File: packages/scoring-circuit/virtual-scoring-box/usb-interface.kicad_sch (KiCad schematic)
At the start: 8 parts, among them J1 GCT USB4105-GF-A, U18 ISOUSB111DWR, U3 TPD2E2U06DCKR

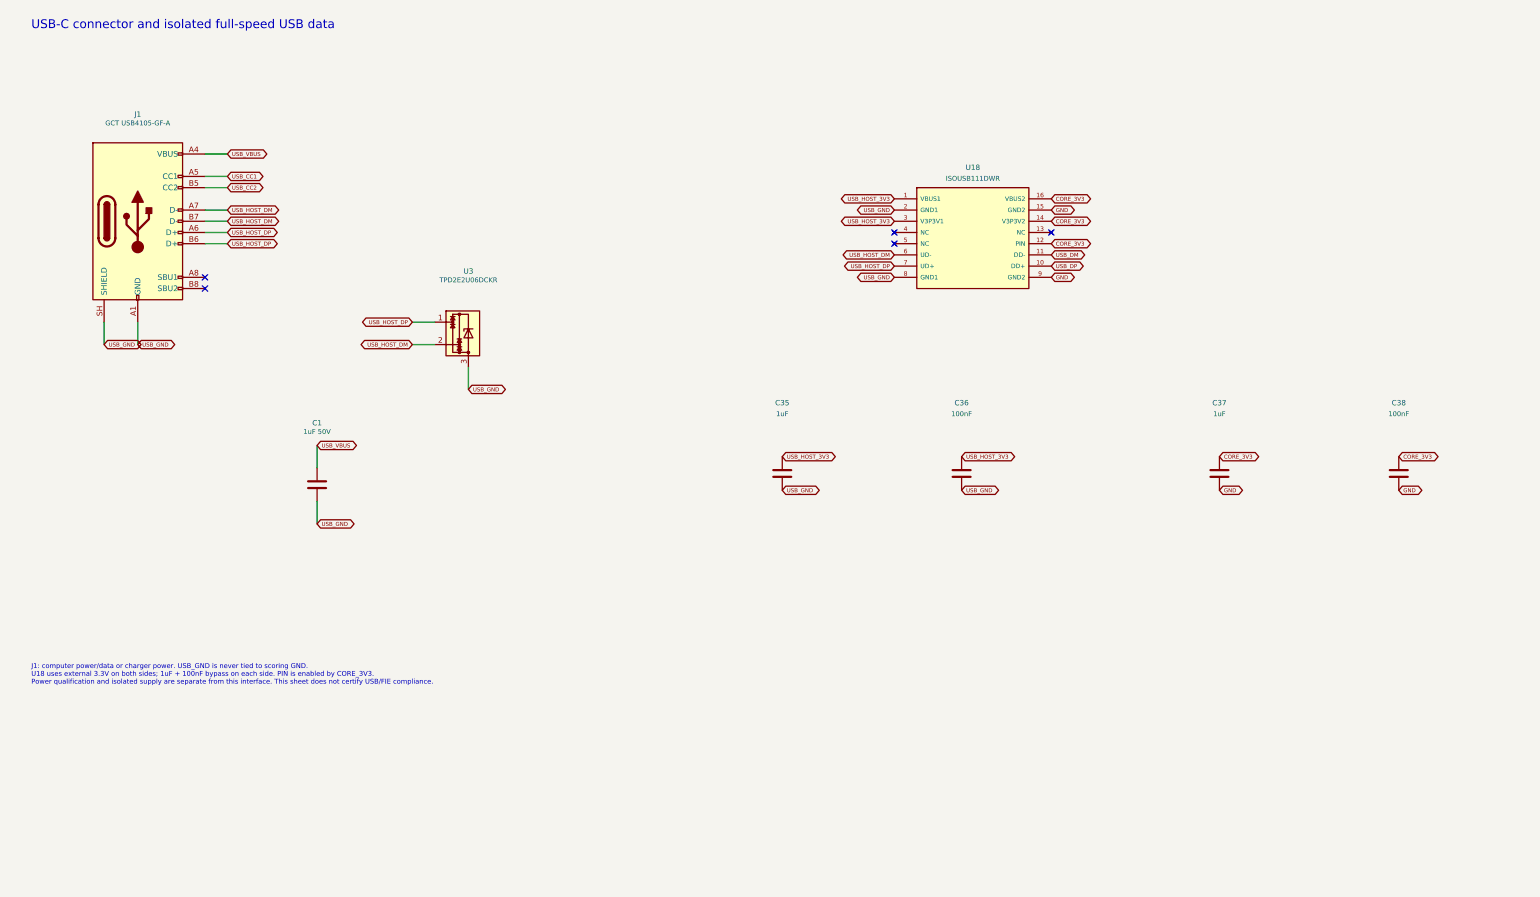
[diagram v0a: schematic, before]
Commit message: feat(scoring-circuit): add suspend-aware isolated serial interface
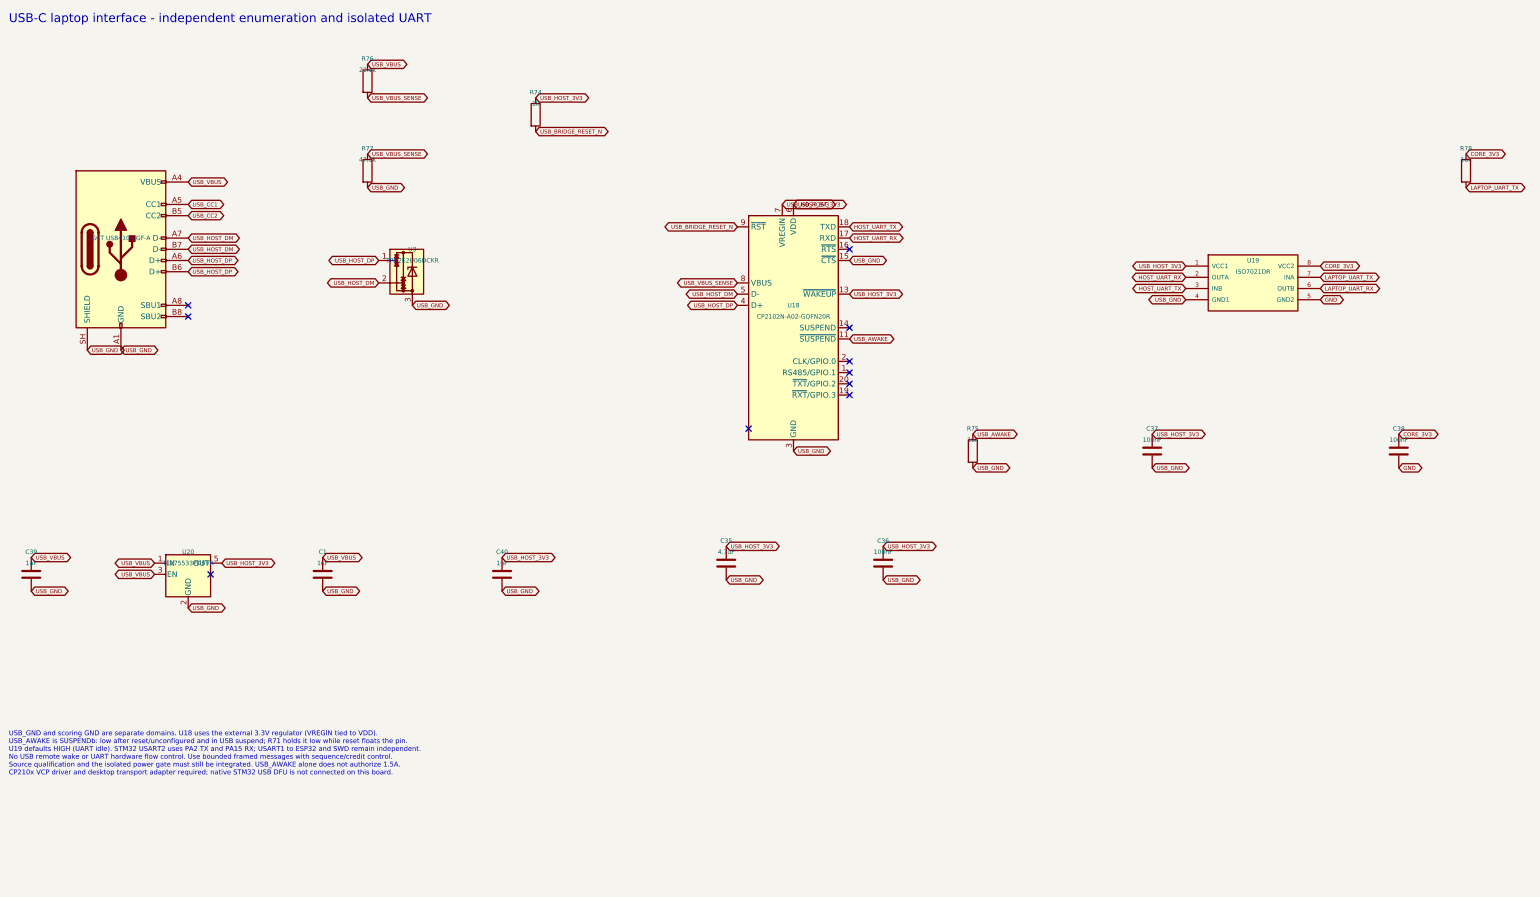
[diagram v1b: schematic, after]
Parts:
- added C39, C40: 1uF, Capacitor_SMD:C_0603_1608Metric, symbol Device:C
- added R74: 1k, Resistor_SMD:R_0603_1608Metric, symbol Device:R
- added R75, R78: 10k, Resistor_SMD:R_0603_1608Metric, symbol Device:R
- added R76: 22.1k, Resistor_SMD:R_0603_1608Metric, symbol Device:R
- added R77: 47.5k, Resistor_SMD:R_0603_1608Metric, symbol Device:R
- added U19: ISO7021DR, Package_SO:SOIC-8_3.9x4.9mm_P1.27mm, symbol ScoringPlatform:ISO7021
- added U20: TLV75533PDBVR, Package_TO_SOT_SMD:SOT-23-5, symbol Regulator_Linear:TLV75533PDBV
- C1: value 1uF 50V -> 1uF; Manufacturer TDK -> (none)
- C35: value 1uF -> 4.7uF; MPN C1608X7R1H105K080AB -> GRM188R61A475KE15D; Manufacturer TDK -> (none)
- C36, C38: Manufacturer Yageo -> (none)
- C37: value 1uF -> 100nF; MPN C1608X7R1H105K080AB -> CC0603KRX7R9BB104; Manufacturer TDK -> (none)
- U18: value ISOUSB111DWR -> CP2102N-A02-GQFN20R; footprint Package_SO:SOIC-16W_7.5x10.3mm_P1.27mm -> ScoringPlatform:CP2102N_QFN20; symbol ScoringPlatform:ISOUSB111 -> Interface_USB:CP2102N-Axx-xQFN20; MPN ISOUSB111DWR -> CP2102N-A02-GQFN20R; Manufacturer Texas Instruments -> Silicon Labs
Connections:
- net CORE_3V3: now also R78.1, U19.8 (VCC2); no longer C37.1, U18.12 (PIN), U18.14 (V3P3V2), U18.16 (VBUS2)
- net GND: now also U19.5 (GND2); no longer C37.2, U18.15 (GND2), U18.9 (GND2)
- net USB_GND: now also C37.2, U18.12 (GND), U18.15 (~{CTS}), U18.21 (GND), U18.3 (GND), C39.2, C40.2, R75.2, R77.2, U19.4 (GND1), U20.2 (GND); no longer U18.2 (GND1), U18.8 (GND1)
- net USB_HOST_3V3: now also C37.1, U18.13 (~{WAKEUP}), U18.6 (VDD), U18.7 (VREGIN), C40.1, R74.1, U19.1 (VCC1), U20.5 (OUT); no longer U18.1 (VBUS1), U18.3 (V3P3V1)
- net USB_HOST_DM: now also U18.5 (D-); no longer U18.6 (UD-)
- net USB_HOST_DP: now also U18.4 (D+); no longer U18.7 (UD+)
- net USB_VBUS: now also C39.1, R76.1, U20.1 (IN), U20.3 (EN)
- net USB_DM renamed USB_AWAKE
- net USB_AWAKE: now also R75.1
- net USB_DP: no longer names the net of U18.10 (NC)
- new net HOST_UART_RX: U18.17 (RXD), U19.2 (OUTA)
- new net HOST_UART_TX: U18.18 (TXD), U19.3 (INB)
- new net LAPTOP_UART_RX: U19.6 (OUTB)
- new net LAPTOP_UART_TX: R78.2, U19.7 (INA)
- new net USB_BRIDGE_RESET_N: R74.2, U18.9 (~{RST})
- new net USB_VBUS_SENSE: R76.2, R77.1, U18.8 (VBUS)
- no-connect marks 5 -> 10
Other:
- note added: "USB-C laptop interface - independent enumeration and isolated UART"
- note added: "USB_GND and scoring GND are separate domains. U18 uses the external 3.3V regulator (VREGIN tied to VDD). USB_AWAKE is SUSPENDb: low after reset/unconfigured and in USB suspend; R71 holds it low while reset floats the pin. U19 defaults HIGH (UART idle). STM32 USART2 uses PA2 TX and PA15 RX; USART1 to ESP32 and SWD remain independent. No USB remote wake or UART hardware flow control. Use bounded fr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"
- note removed: "J1: computer power/data or charger power. USB_GND is never tied to scoring GND. U18 uses external 3.3V on both sides; 1uF + 100nF bypass on each side. PIN is enabled by CORE_3V3. Power qualification and isolated supply are separate from this interface. This sheet does not certify USB/FIE compliance."
- note removed: "USB-C connector and isolated full-speed USB data"
- title: USB-C connector and isolated data -> USB-C serial bridge and isolated laptop interface
- moved on the sheet: C1, C35, C36, C37, C38, J1, U18, U3

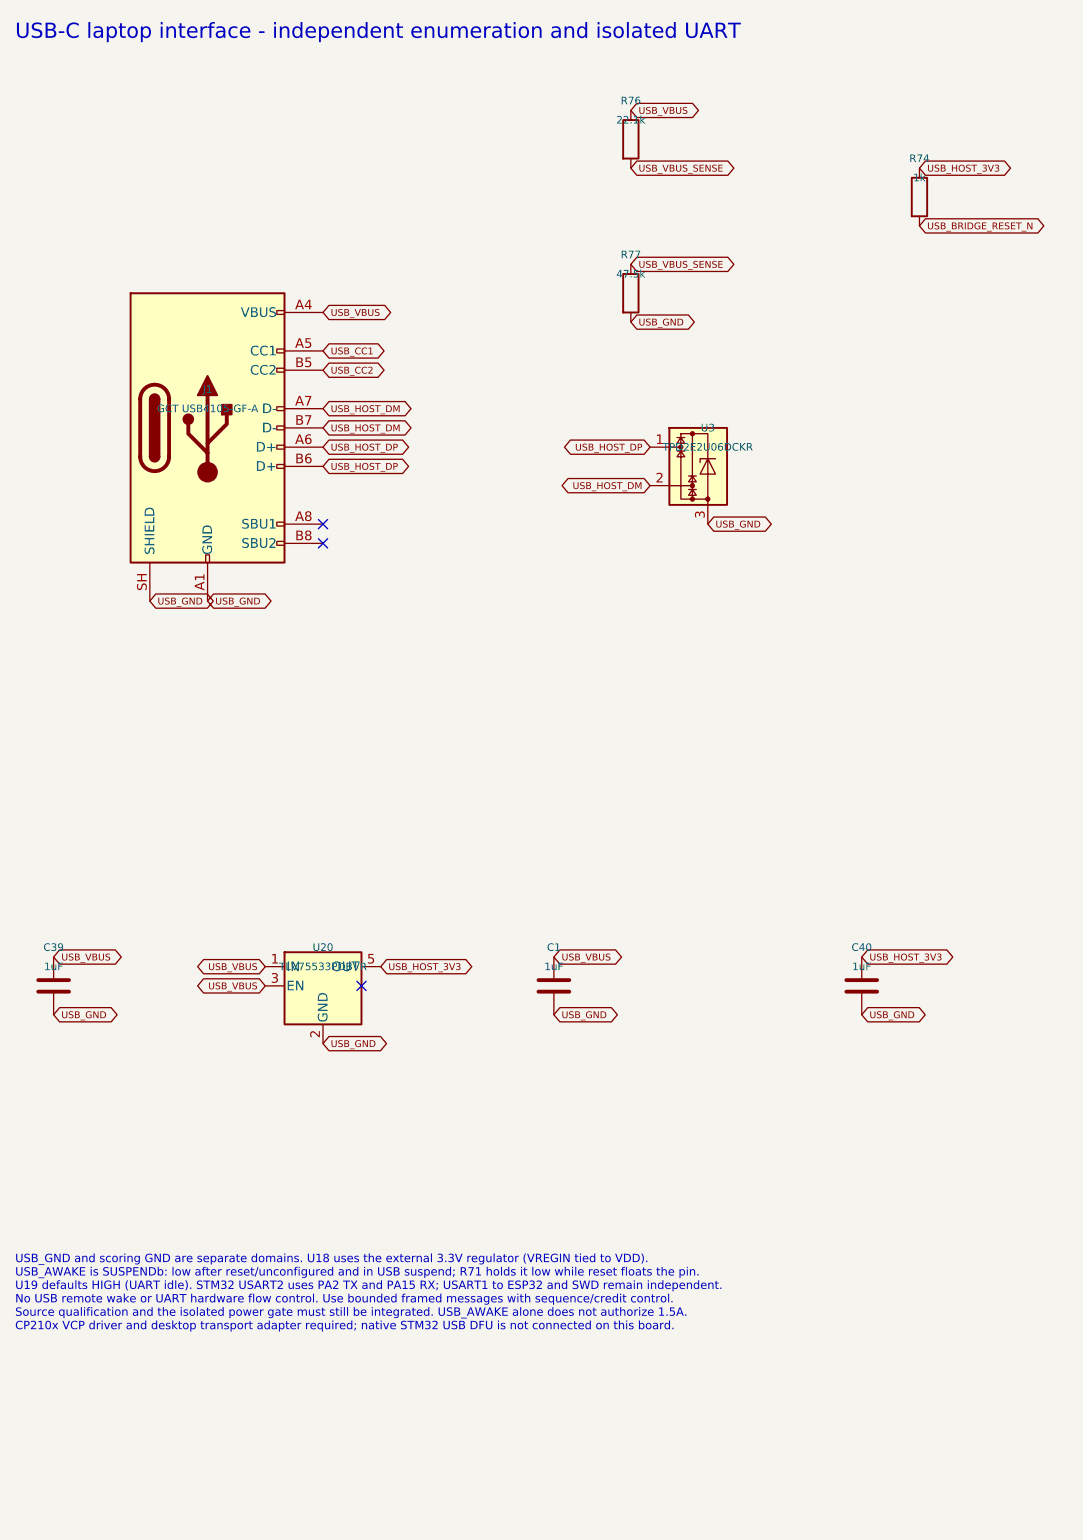
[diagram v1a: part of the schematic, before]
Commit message: feat(scoring-circuit): integrate virtual-box USB-C source control
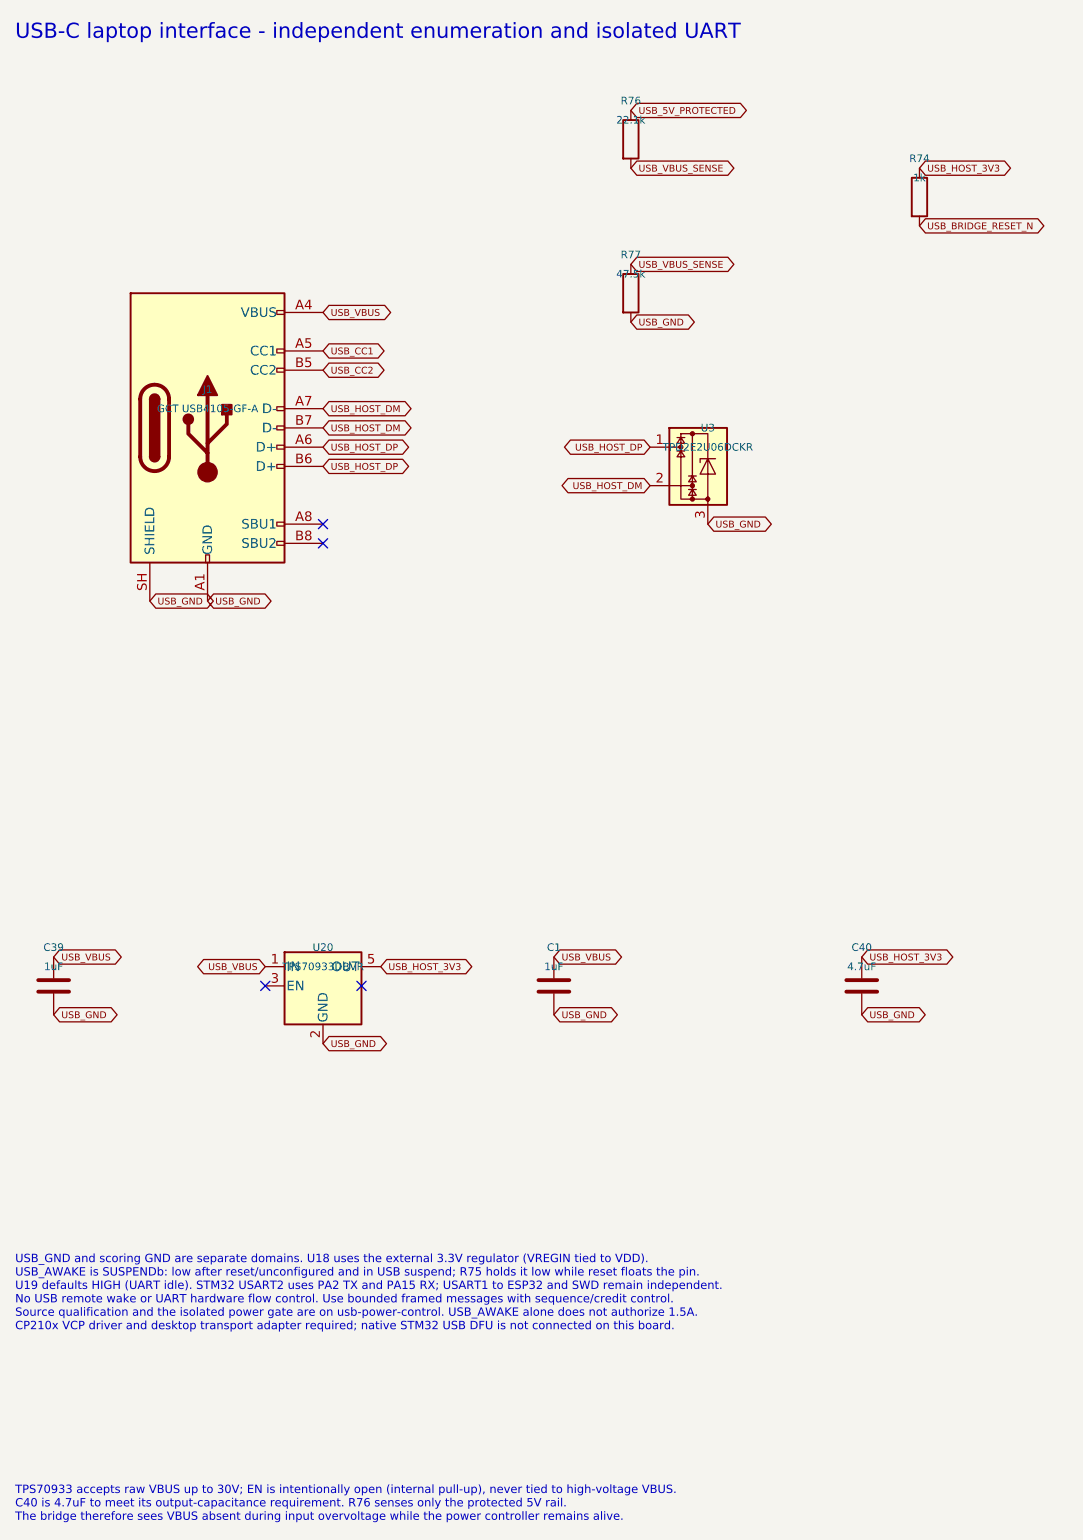
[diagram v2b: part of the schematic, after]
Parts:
- C40: value 1uF -> 4.7uF; MPN C1608X7R1H105K080AB -> GRM188R61A475KE15D; Manufacturer (none) -> Murata
- U20: value TLV75533PDBVR -> TPS70933DBVR; symbol Regulator_Linear:TLV75533PDBV -> ScoringPlatform:TPS70933DBV; MPN TLV75533PDBVR -> TPS70933DBVR
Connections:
- net USB_VBUS: no longer R76.1, U20.3 (EN)
- new net USB_5V_PROTECTED: R76.1
- no-connect marks 10 -> 11
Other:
- note added: "TPS70933 accepts raw VBUS up to 30V; EN is intentionally open (internal pull-up), never tied to high-voltage VBUS. C40 is 4.7uF to meet its output-capacitance requirement. R76 senses only the protected 5V rail. The bridge therefore sees VBUS absent during input overvoltage while the power controller remains alive."
- note added: "USB_GND and scoring GND are separate domains. U18 uses the external 3.3V regulator (VREGIN tied to VDD). USB_AWAKE is SUSPENDb: low after reset/unconfigured and in USB suspend; R75 holds it low while reset floats the pin. U19 defaults HIGH (UART idle). STM32 USART2 uses PA2 TX and PA15 RX; USART1 to ESP32 and SWD remain independent. No USB remote wake or UART hardware flow control. Use bounded fr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"
- note removed: "USB_GND and scoring GND are separate domains. U18 uses the external 3.3V regulator (VREGIN tied to VDD). USB_AWAKE is SUSPENDb: low after reset/unconfigured and in USB suspend; R71 holds it low while reset floats the pin. U19 defaults HIGH (UART idle). STM32 USART2 uses PA2 TX and PA15 RX; USART1 to ESP32 and SWD remain independent. No USB remote wake or UART hardware flow control. Use bounded fr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"

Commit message: feat(scoring-circuit): simplify virtual-box UART and export assembly handoff
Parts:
- C1, C39: Manufacturer (none) -> TDK
- C35: Manufacturer (none) -> Murata
- C36, C37, C38: Manufacturer (none) -> Yageo
